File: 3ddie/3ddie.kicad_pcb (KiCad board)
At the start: 2 copper layers, 150 x 180 mm, 57 parts, among them J1 USB4105-GF-A, J2 TRS_MIDI_IN, J3 TRS_MIDI_OUT, J4 Conn_02x15_Odd_Even, U1 W25Q128JV, U2 RP2040, U3 MCP1702T-3302E_CB, U4 MGC3130-I/MQ, U5 MCP1416R, U6 6N137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

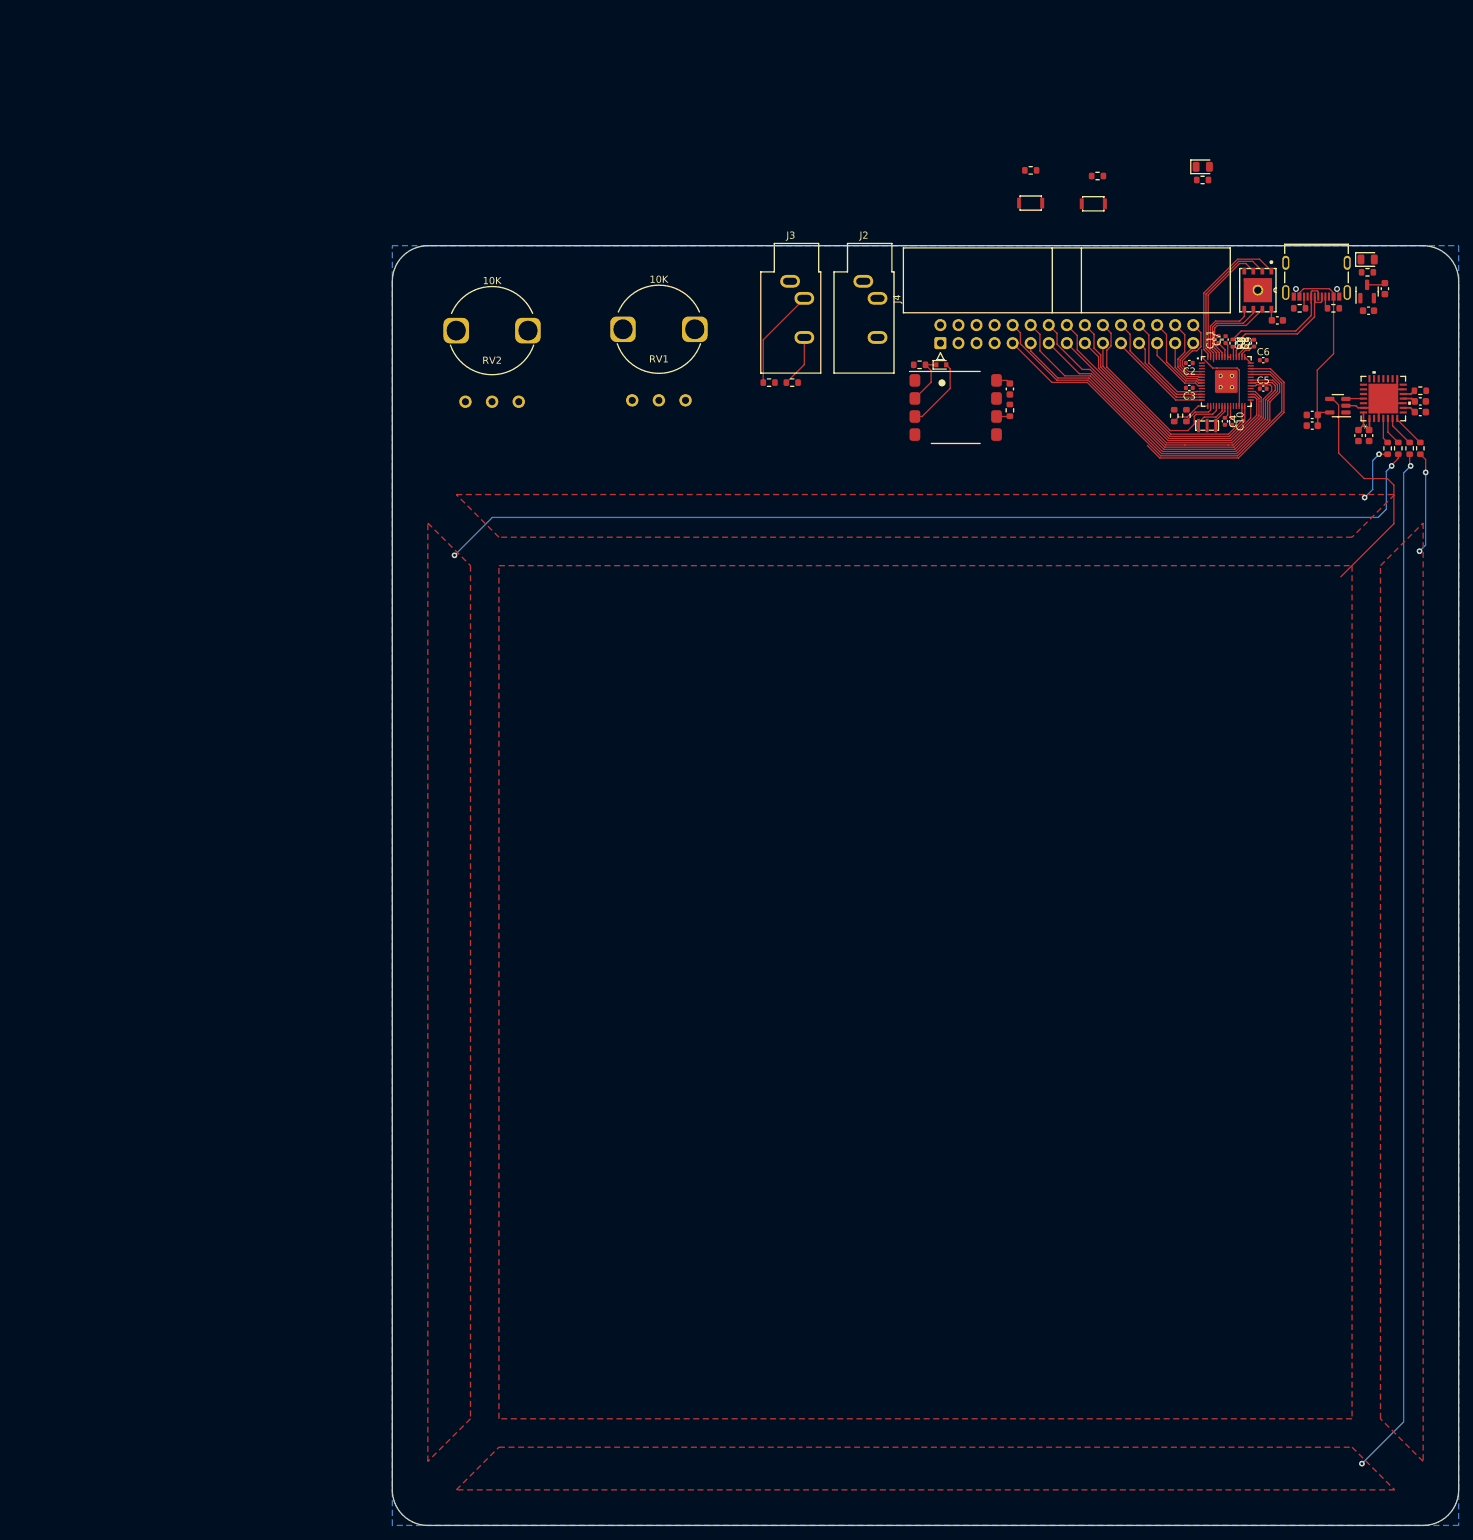
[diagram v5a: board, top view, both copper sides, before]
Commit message: mostly finish routing and layout!
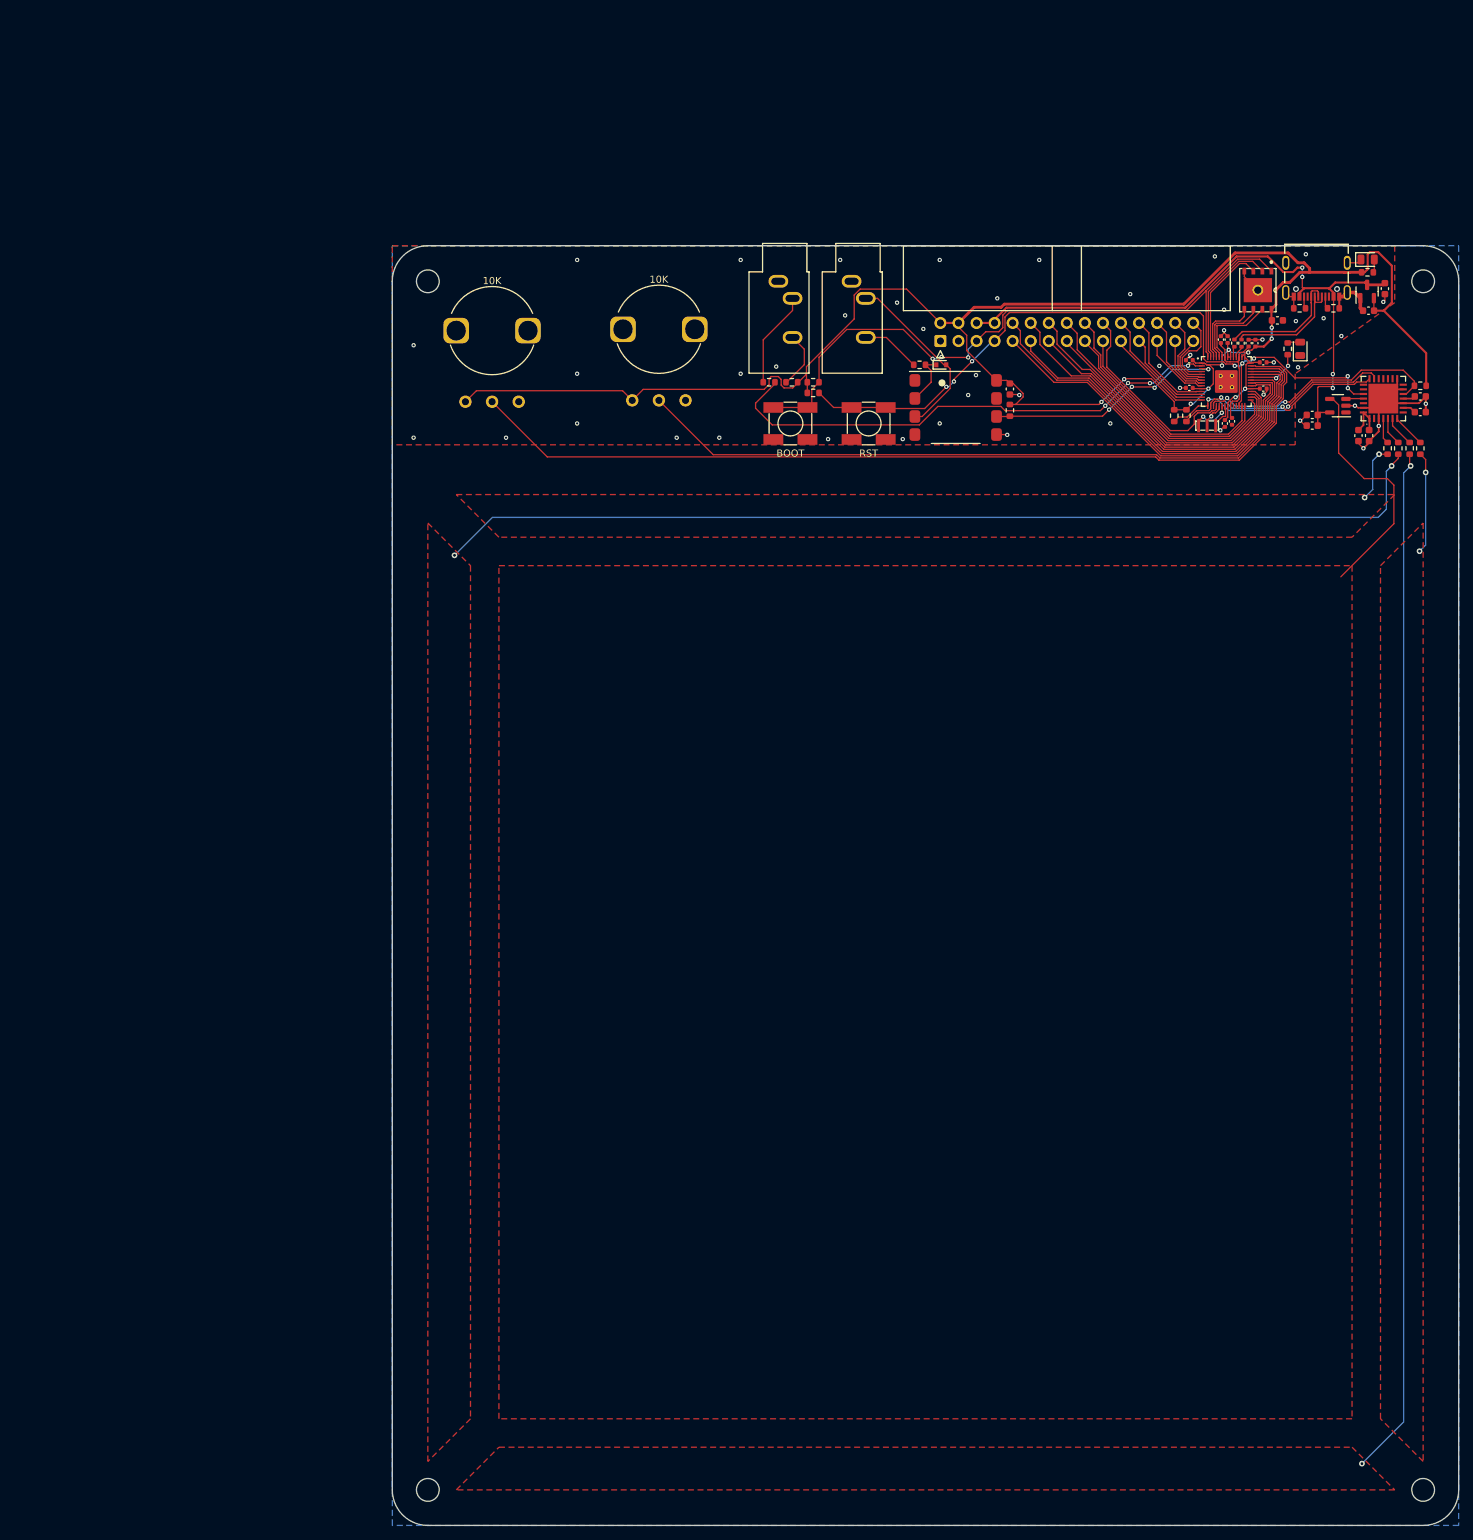
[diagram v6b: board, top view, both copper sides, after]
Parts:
- added REF**: MountingHole_3.2mm_M3, MountingHole:MountingHole_3.2mm_M3, F.Cu at (165.0, 191.0)
- added REF**: MountingHole_3.2mm_M3, MountingHole:MountingHole_3.2mm_M3, F.Cu at (25.0, 21.0)
- added REF**: MountingHole_3.2mm_M3, MountingHole:MountingHole_3.2mm_M3, F.Cu at (165.0, 21.0)
- added REF**: MountingHole_3.2mm_M3, MountingHole:MountingHole_3.2mm_M3, F.Cu at (25.0, 191.0)
- S1, S2: footprint Eclectronics:KXT321LHS -> Eclectronics:TL3301AFxxxxJ
- moved R2 50.3 mm to (79.2, 36.7), turned to 180 degrees
- moved S2 45.9 mm to (76.0, 41.0)
- moved S1 44.2 mm to (87.0, 41.0)
- moved R3 42.7 mm to (79.2, 35.2), turned to 180 degrees
- moved D1 29.0 mm to (147.7, 30.5), turned to 90 degrees
- moved R7 26.6 mm to (145.9, 30.5), turned to 90 degrees
- moved J3 1.65 mm to (74.3, 21.0)
- moved J2 1.65 mm to (84.6, 21.0)
- moved C16 0.70 mm to (164.6, 37.2)
- moved R13 0.70 mm to (164.6, 35.7)
- moved C2 0.40 mm to (132.1, 32.1)
- moved C11 0.34 mm to (136.6, 29.2)
- moved C6 0.30 mm to (142.5, 32.4)
- moved J4 0.30 mm to (97.1, 29.4)
- moved C4 0.30 mm to (137.1, 41.0)
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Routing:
- net +3V3: track 11.8 -> 282.5 mm, vias 0 -> 11
- net /POT2: track 0.00 -> 129.0 mm
- net /RUN: track 12.2 -> 100.9 mm, vias 0 -> 8
- net /BOOT: track 21.4 -> 97.2 mm, vias 0 -> 3
- net /MIDI_TX: track 0.00 -> 72.7 mm, vias 0 -> 4
- net /POT1: track 32.3 -> 104.4 mm
- net /VBUS: track 29.9 -> 91.4 mm, vias 0 -> 4
- net GND: track 19.3 -> 65.8 mm, vias 0 -> 49
- net /EIO0: track 1.77 -> 34.9 mm, vias 0 -> 2
- net /MIDI_RX: track 1.90 -> 33.6 mm, vias 0 -> 4
- net /EIO4/SI0: track 5.63 -> 33.3 mm, vias 0 -> 2
- net /EIO5/SI1: track 4.70 -> 30.8 mm, vias 0 -> 2
- net Net-(D3-Pad2): track 10.1 -> 25.3 mm
- net Net-(C10-Pad1): track 6.11 -> 17.1 mm
- net Net-(J2-PadR): track 0.00 -> 8.34 mm
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- added copper zone on F.Cu, net GND
